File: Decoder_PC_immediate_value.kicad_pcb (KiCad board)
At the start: 2 copper layers, 66.4 x 62.6 mm, 1 part

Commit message: Added /WE
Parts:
- added C1: 0.1µF, Capacitor_SMD:C_0805_2012Metric_Pad1.18x1.45mm_HandSolder, F.Cu at (93.9, 88.5)
- added R1: 330Ω, Resistor_SMD:R_0805_2012Metric_Pad1.20x1.40mm_HandSolder, F.Cu at (90.7, 88.7)
- added TP1: /WE, TestPoint:TestPoint_Pad_D1.0mm, B.Cu at (90.8, 87.7)
- turned U1 to 180 degrees
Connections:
- U1 pad 13: unconnected-(U1-DQ0-Pad13) -> ControlWord0
- U1 pad 14: unconnected-(U1-DQ1-Pad14) -> ControlWord1
- U1 pad 15: unconnected-(U1-DQ2-Pad15) -> ControlWord2
- U1 pad 16: unconnected-(U1-Vss-Pad16) -> GND
- U1 pad 17: unconnected-(U1-DQ3-Pad17) -> ControlWord3
- U1 pad 18: unconnected-(U1-DQ4-Pad18) -> ControlWord4
- U1 pad 19: unconnected-(U1-DQ5-Pad19) -> ControlWord5
- U1 pad 20: unconnected-(U1-DQ6-Pad20) -> ControlWord6
- U1 pad 21: unconnected-(U1-DQ7-Pad21) -> ControlWord7
- U1 pad 22: unconnected-(U1-CE#-Pad22) -> /CE
- U1 pad 24: unconnected-(U1-OE#-Pad24) -> /OE
- U1 pad 31: unconnected-(U1-WE#-Pad31) -> /WE
- U1 pad 32: unconnected-(U1-Vdd-Pad32) -> VCC
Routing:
- net VCC: track 0.00 -> 9.85 mm
- net /WE: track 0.00 -> 9.06 mm, vias 0 -> 1
- net GND: track 0.00 -> 4.10 mm, vias 0 -> 2
- added copper zone on B.Cu, net (none)
- added copper zone on F.Cu, net (none)
- added copper zone on In1.Cu, net (none)
- added copper zone on In2.Cu, net GND
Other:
- copper layers 2 -> 4
- board text added: "/WE"

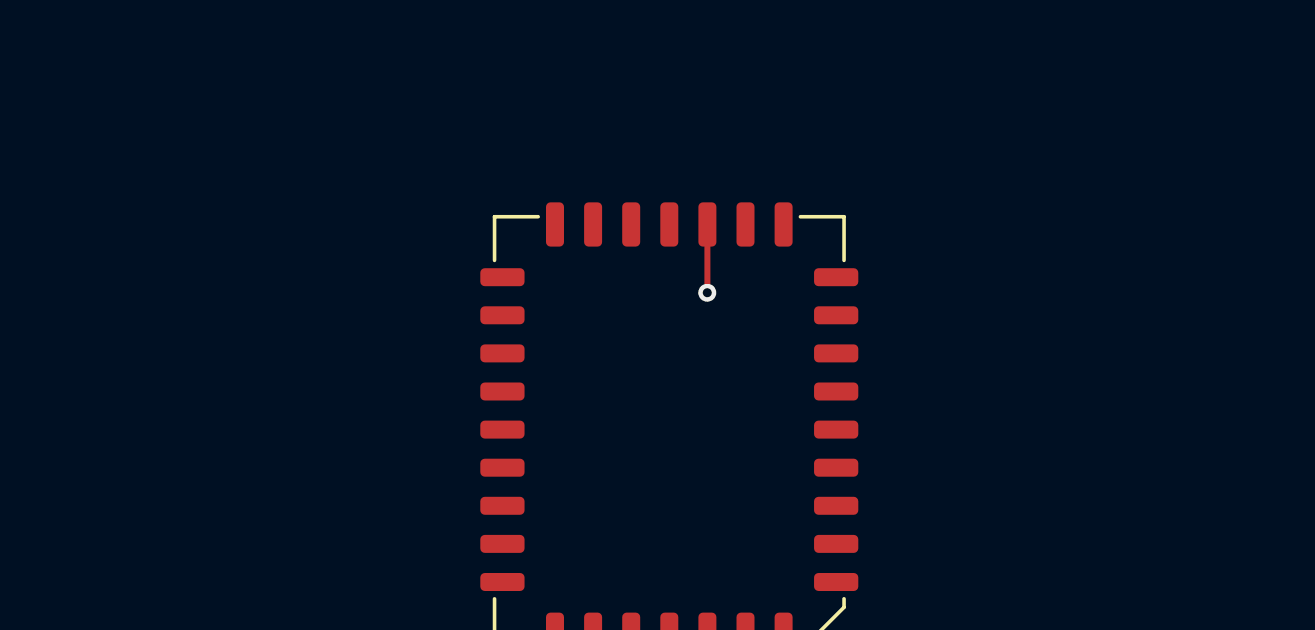
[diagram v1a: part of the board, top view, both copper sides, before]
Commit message: Added default pulls for /WE, /CE & /OE
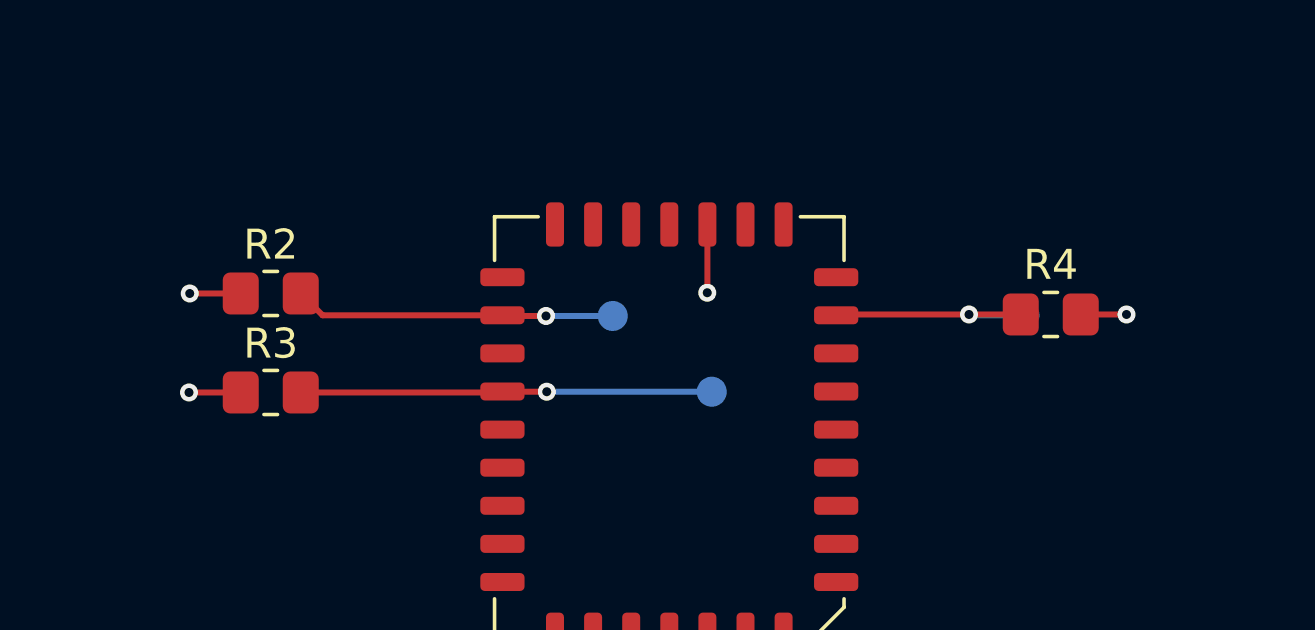
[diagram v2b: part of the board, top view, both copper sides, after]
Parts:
- added R2: 330Ω, Resistor_SMD:R_0805_2012Metric_Pad1.20x1.40mm_HandSolder, F.Cu at (81.4, 70.6)
- added R3: 330Ω, Resistor_SMD:R_0805_2012Metric_Pad1.20x1.40mm_HandSolder, F.Cu at (81.4, 73.9)
- added R4: 330Ω, Resistor_SMD:R_0805_2012Metric_Pad1.20x1.40mm_HandSolder, F.Cu at (107.4, 71.3)
- added TP2: /CE, TestPoint:TestPoint_Pad_D1.0mm, B.Cu at (92.8, 71.4)
- added TP3: /OE, TestPoint:TestPoint_Pad_D1.0mm, B.Cu at (96.1, 73.9)
- added TP4: AUX1, TestPoint:TestPoint_Pad_D1.0mm, B.Cu at (106.5, 71.3)
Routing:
- net /OE: track 0.00 -> 13.7 mm, vias 0 -> 1
- net /CE: track 0.00 -> 10.7 mm, vias 0 -> 1
- net AUX_1: track 0.00 -> 8.02 mm, vias 0 -> 1
- net GND: track 4.10 -> 9.05 mm, vias 2 -> 5
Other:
- board text added: "/CE"
- board text added: "/OE"
- board text added: "AUX1"
